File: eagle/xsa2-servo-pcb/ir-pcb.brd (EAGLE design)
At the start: 96 x 85 mm, 62 parts, among them IC1 ATMEGA328P-AU, IC10 SK6812_SIDE, IC11 SK6812_SIDE, IC12 SK6812_SIDE, IC13 SK6812_SIDE, IC14 SK6812_SIDE, IC15 SK6812_SIDE, IC16 SK6812_SIDE, IC17 SK6812_SIDE, IC18 SK6812_SIDE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

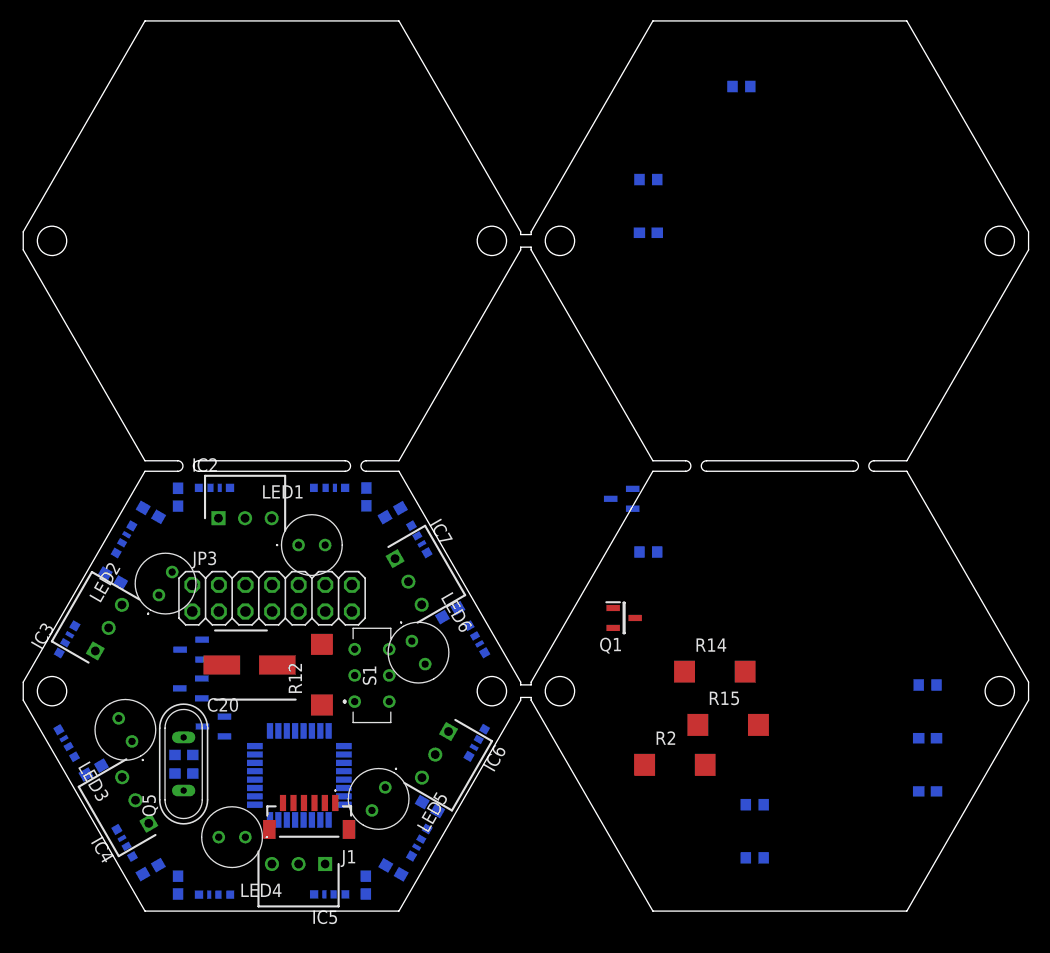
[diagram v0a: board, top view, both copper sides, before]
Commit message: [eagle] IR基板の更新
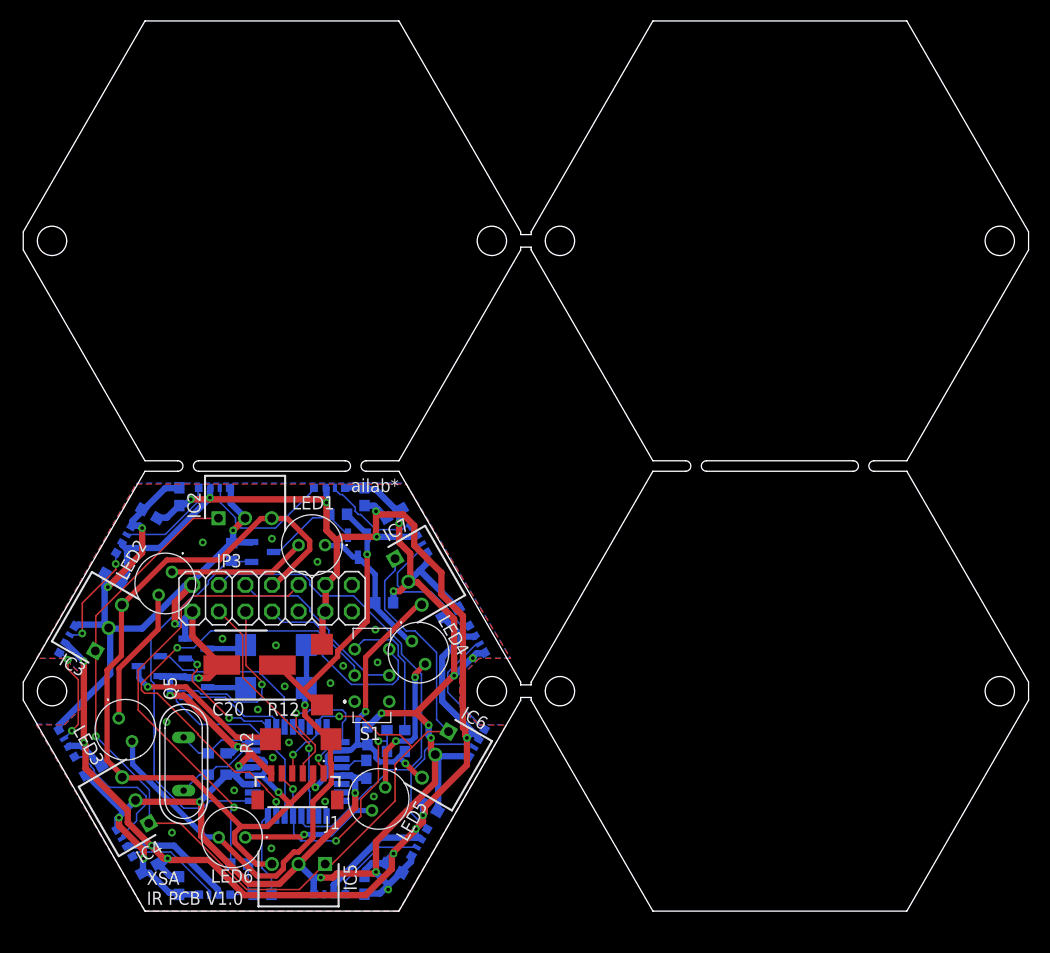
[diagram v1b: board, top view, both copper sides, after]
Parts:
- moved R7 59.7 mm to (35.6, 15.2)
- moved R1 56.1 mm to (30.1, 37.9)
- moved C5 55.0 mm to (32.9, 16.7), turned to 270 degrees
- moved C2 53.6 mm to (32.8, 13.5), turned to 90 degrees
- moved R6 52.5 mm to (34.5, 29.4)
- moved C1 50.8 mm to (35.6, 17.3)
- moved R10 49.6 mm to (20.6, 4.50)
- moved R11 47.1 mm to (22.9, 1.60), turned to 180 degrees
- moved R15 43.3 mm to (24.1, 21.3), flipped to the bottom, turned to 180 degrees
- moved R14 42.0 mm to (24.1, 25.4), flipped to the bottom, turned to 180 degrees
- moved R9 39.8 mm to (19.9, 34.3), turned to 270 degrees
- moved R2 35.8 mm to (26.5, 16.4)
- moved Q6 34.7 mm to (22.9, 34.3), turned to 180 degrees
- moved Q1 26.3 mm to (32.0, 34.8), flipped to the bottom, turned to 270 degrees
- moved LED6 24.6 mm to (21.2, 7.04), turned to 180 degrees
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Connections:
- net N$12 renamed LED7
- net N$15 renamed LED8
- net N$16 renamed LED9
- net N$17 renamed LED10
- net N$27 renamed LED2
- net N$4 renamed LED1
- net N$6 renamed LED4
- net N$7 renamed LED6
- net N$8 renamed LED3
- net N$9 renamed LED5
- removed net N$35: IC13.3, IC14.1
- new net N$11: IC8.1, IC9.3
- net N$24: now also IC13.1, IC14.3; no longer IC8.3, IC9.1
- net N$31: now also IC12.1, IC13.3; no longer IC10.1, IC9.3
- net N$32: now also IC12.3; no longer IC10.3
- net N$33: now also IC10.1; no longer IC12.1
- net N$34: now also IC10.3, IC9.1; no longer IC12.3, IC13.1
- net N$36: now also IC19.1, IC8.3; no longer IC14.3, IC15.1
- net N$37: now also IC18.1, IC19.3; no longer IC15.3, IC16.1
- net N$38: now also IC18.3; no longer IC16.3
- net N$39: now also IC16.1; no longer IC18.1
- net N$40: now also IC15.1, IC16.3; no longer IC18.3, IC19.1
- net N$44: now also IC14.1; no longer IC8.1
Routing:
- net GND: track 0.00 -> 258.1 mm, vias 0 -> 41
- net VDD: track 0.00 -> 205.7 mm, vias 0 -> 13
- net +3V3: track 0.00 -> 114.5 mm, vias 0 -> 4
- net N$41: track 0.00 -> 113.7 mm, vias 0 -> 3
- net N$29: track 0.00 -> 52.8 mm, vias 0 -> 2
- net N$21: track 0.00 -> 47.4 mm
- net LED7: track 0.00 -> 46.1 mm, vias 0 -> 1
- net N$42: track 0.00 -> 42.3 mm, vias 0 -> 1
- net N$10: track 0.00 -> 37.3 mm
- net N$23: track 0.00 -> 36.6 mm, vias 0 -> 1
- net LED2: track 0.00 -> 26.1 mm, vias 0 -> 1
- net N$25: track 0.00 -> 24.7 mm, vias 0 -> 3
- net N$30: track 0.00 -> 23.1 mm, vias 0 -> 1
- net N$3: track 0.00 -> 17.8 mm
- net N$20: track 0.00 -> 16.3 mm
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- added copper zone on layer 1, net GND
- added copper zone on layer 16, net GND
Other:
- board text added: "XSA IR PCB V1.0"
- board text added: "ailab*"
